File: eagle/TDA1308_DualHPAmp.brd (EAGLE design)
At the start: 33.1 x 66.1 mm, 28 parts, among them IC1 TDA1308, IC2 TDA1308, IC3 TLE2426CLP

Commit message: update board design
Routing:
- net GND: track 221.7 -> 216.7 mm
- net N$5: track 31.3 -> 29.1 mm
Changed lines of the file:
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@@
 <contactref element="C7" pad="2"/>
 <contactref element="C4" pad="-"/>
-<wire x1="18.17" y1="23.102878125" x2="15.596984375" y2="23.0698625" width="0.4064" layer="16"/>
 <wire x1="2.8492625" y1="23.0698625" x2="2.7062" y2="22.9268" width="0.4064" layer="16"/>
 <wire x1="2.7062" y1="35.7768" x2="2.7062" y2="22.9268" width="0.4064" layer="16"/>
-<wire x1="17.99" y1="22.922878125" x2="15.596984375" y2="23.0698625" width="0.4064" layer="16"/>
 <wire x1="18.041509375" y1="35.98429375" x2="17.99429375" y2="35.98429375" width="0.4064" layer="16"/>
 <wire x1="17.99429375" y1="35.98429375" x2="17.99" y2="35.98" width="0.4064" layer="16"/>
@@
 <wire x1="25.7" y1="43.72" x2="25.7" y2="41.18" width="0.4064" layer="16"/>
 <wire x1="25.7" y1="41.18" x2="25.76" y2="41.12" width="0.4064" layer="16"/>
-<wire x1="25.73" y1="33.38" x2="27.94" y2="33.38" width="0.4064" layer="16"/>
 <wire x1="25.76" y1="41.12" x2="25.76" y2="33.41" width="0.4064" layer="16"/>
 <wire x1="25.76" y1="33.41" x2="25.73" y2="33.38" width="0.4064" layer="16"/>

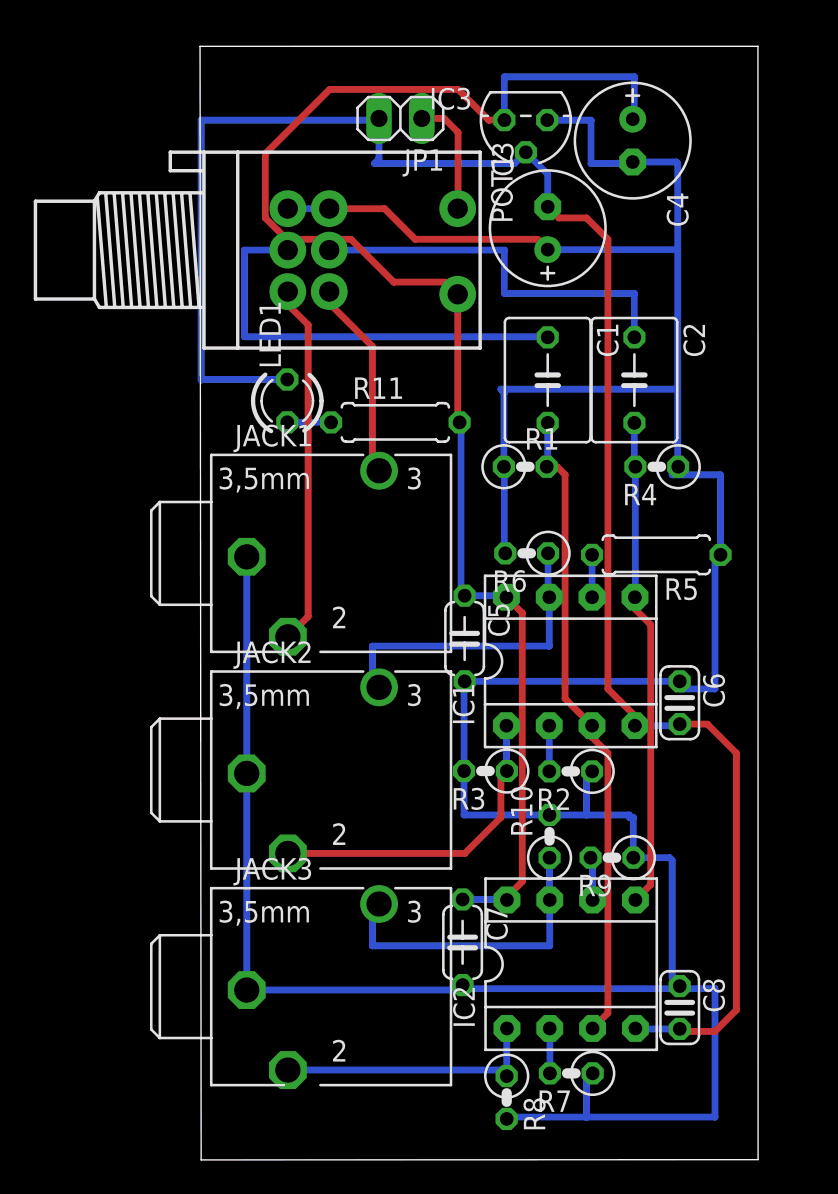
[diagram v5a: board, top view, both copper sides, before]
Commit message: 非反転増幅回路のRの位置を修正
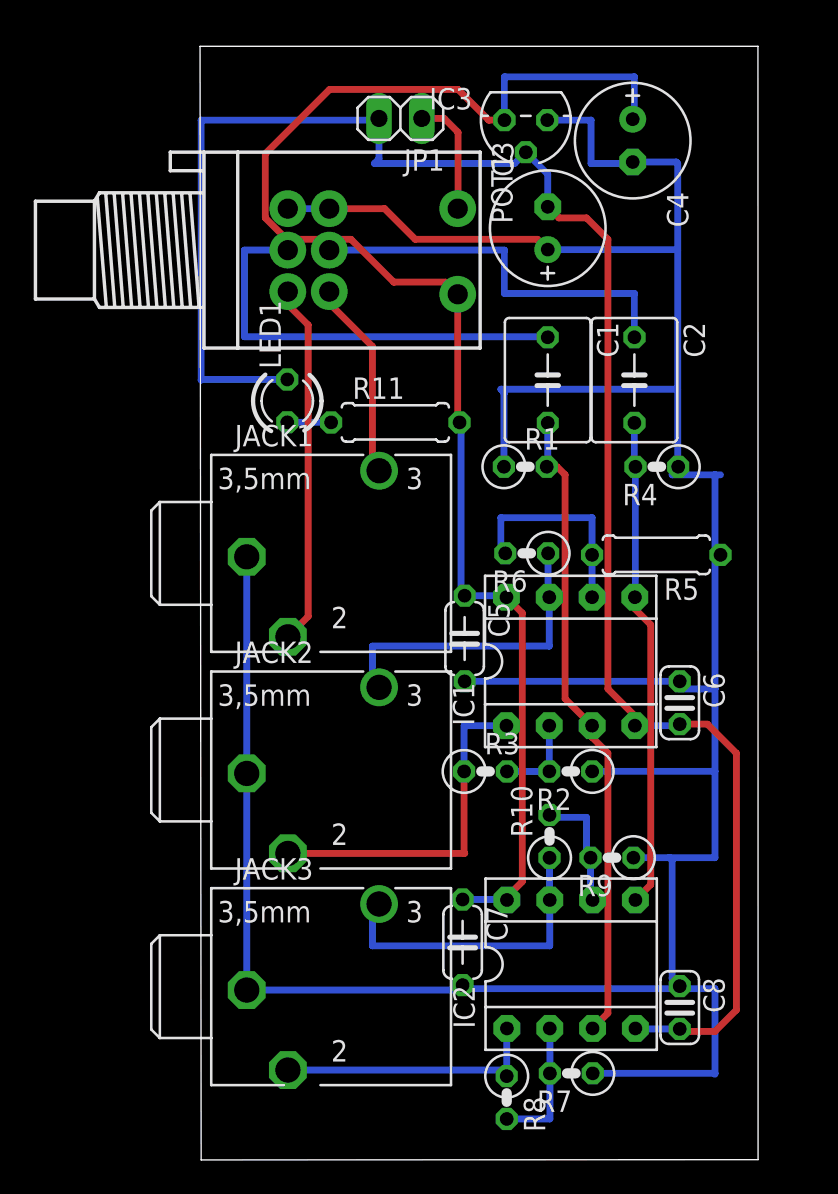
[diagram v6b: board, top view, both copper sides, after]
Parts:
- turned R3 to 0 degrees
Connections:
- removed net N$15: IC2.2, R7.2
- removed net N$17: IC2.6, R9.2
- new net N$12: IC2.2, R7.2, R8.2
- new net N$14: IC2.6, R10.2, R9.2
- net GND: no longer R10.2, R3.2, R6.2, R8.2
- net N$7: now also R3.2
- net N$9: now also R6.2
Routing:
- net GND: track 216.7 -> 197.3 mm
- net N$9: track 2.51 -> 12.5 mm
- net N$12: track 0.00 -> 7.94 mm
- net N$14: track 0.00 -> 7.60 mm
- net N$15: track 2.67 -> 0.00 mm
- net N$17: track 2.56 -> 0.00 mm
- net N$7: track 3.38 -> 5.24 mm
- net N$8: track 19.1 -> 20.6 mm
